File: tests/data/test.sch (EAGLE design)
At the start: 2 parts

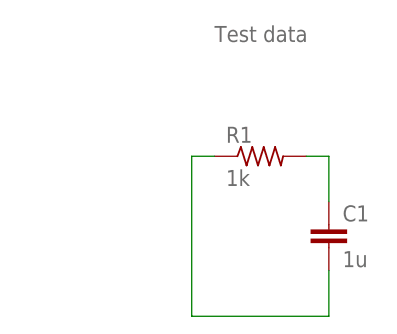
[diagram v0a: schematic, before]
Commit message: Update test data
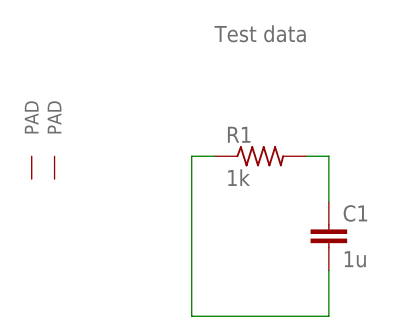
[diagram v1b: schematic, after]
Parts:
- added U$1: PADLONG, pad:PADLONG
- added U$2: PADOFFSET, pad:PADOFFSET
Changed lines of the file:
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@@
 <part name="C1" library="rcl" deviceset="C-EU" device="C0402" value="1u"/>
 <part name="R1" library="rcl" deviceset="R-US_" device="R0402" value="1k"/>
+<part name="U$1" library="pad" deviceset="PAD" device="LONG"/>
+<part name="U$2" library="pad" deviceset="PAD" device="OFFSET"/>
 </parts>
 <sheets>
@@
 <instance part="C1" gate="G$1" x="101.6" y="73.66"/>
 <instance part="R1" gate="G$1" x="93.98" y="81.28"/>
+<instance part="U$1" gate="G" x="71.12" y="81.28" rot="R90"/>
+<instance part="U$2" gate="G" x="68.58" y="81.28" rot="R90"/>
 </instances>
 <busses>

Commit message: Update test data
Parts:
- renumbered U$1 to PAD1, U$2 to PAD2
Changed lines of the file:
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@@
 <part name="C1" library="rcl" deviceset="C-EU" device="C0402" value="1u"/>
 <part name="R1" library="rcl" deviceset="R-US_" device="R0402" value="1k"/>
-<part name="U$1" library="pad" deviceset="PAD" device="LONG"/>
-<part name="U$2" library="pad" deviceset="PAD" device="OFFSET"/>
+<part name="PAD1" library="pad" deviceset="PAD" device="LONG"/>
+<part name="PAD2" library="pad" deviceset="PAD" device="OFFSET"/>
 </parts>
 <sheets>
@@
 <instance part="C1" gate="G$1" x="101.6" y="73.66"/>
 <instance part="R1" gate="G$1" x="93.98" y="81.28"/>
-<instance part="U$1" gate="G" x="71.12" y="81.28" rot="R90"/>
-<instance part="U$2" gate="G" x="68.58" y="81.28" rot="R90"/>
+<instance part="PAD1" gate="G" x="71.12" y="81.28" rot="R90"/>
+<instance part="PAD2" gate="G" x="68.58" y="81.28" rot="R90"/>
 </instances>
 <busses>

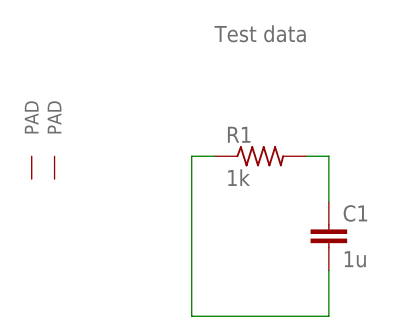
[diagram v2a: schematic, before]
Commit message: Add rotated pad to test data
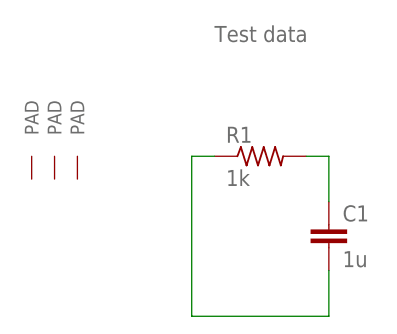
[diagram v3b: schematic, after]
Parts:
- added PAD3: PADOFFSET, pad:PADOFFSET
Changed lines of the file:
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@@
 <part name="PAD1" library="pad" deviceset="PAD" device="LONG"/>
 <part name="PAD2" library="pad" deviceset="PAD" device="OFFSET"/>
+<part name="PAD3" library="pad" deviceset="PAD" device="OFFSET"/>
 </parts>
 <sheets>
@@
 <instance part="PAD1" gate="G" x="71.12" y="81.28" rot="R90"/>
 <instance part="PAD2" gate="G" x="68.58" y="81.28" rot="R90"/>
+<instance part="PAD3" gate="G" x="73.66" y="81.28" rot="R90"/>
 </instances>
 <busses>
